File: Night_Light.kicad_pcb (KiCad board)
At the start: 2 copper layers, 27.9 x 27.9 mm, 10 parts, among them J1 3V0, Q1 2N3904

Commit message: Finished wiring the PCB
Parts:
- moved R3 0.25 mm to (128.8, 88.4)
- moved R2 0.22 mm to (145.9, 93.5)
- moved R1 0.14 mm to (128.8, 93.5)
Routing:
- net +3V0: track 0.00 -> 17.1 mm
- net /Base: track 0.00 -> 13.4 mm
- net /LED +: track 0.00 -> 5.40 mm
- net /Collecter: track 0.00 -> 4.98 mm
- added copper zone on B.Cu, net GND
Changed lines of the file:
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@@
   )
   (footprint "Resistor_THT:R_Axial_DIN0207_L6.3mm_D2.5mm_P10.16mm_Horizontal" (layer "F.Cu")
-    (at 128.524 88.392)
+    (at 128.778 88.392)
     (descr "Resistor, Axial_DIN0207 series, Axial, Horizontal, pin pitch=10.16mm, 0.25W = 1/4W, length*diameter=6.3*2.5mm^2, http://cdn-reichelt.de/documents/datenblatt/B400/1_4W%23YAG.pdf")
     (tags "Resistor Axial_DIN0207 series Axial Horizontal pin pitch 10.16mm 0.25W = 1/4W length 6.3mm diameter 2.5mm")
@@
   )
   (footprint "Resistor_THT:R_Axial_DIN0207_L6.3mm_D2.5mm_P10.16mm_Horizontal" (layer "F.Cu")
-    (at 128.92 93.5)
+    (at 128.778 93.472)
     (descr "Resistor, Axial_DIN0207 series, Axial, Horizontal, pin pitch=10.16mm, 0.25W = 1/4W, length*diameter=6.3*2.5mm^2, http://cdn-reichelt.de/documents/datenblatt/B400/1_4W%23YAG.pdf")
     (tags "Resistor Axial_DIN0207 series Axial Horizontal pin pitch 10.16mm 0.25W = 1/4W length 6.3mm diameter 2.5mm")
@@
   )
   (footprint "OptoDevice:R_LDR_4.9x4.2mm_P2.54mm_Vertical" (layer "F.Cu")
-    (at 145.94 93.25)
+    (at 145.94 93.472)
     (descr "Resistor, LDR 4.9x4.2mm")
     (tags "Resistor LDR4.9x4.2")
@@
   (gr_line (start 140.97 73.66) (end 140.97 106.68) (layer "Cmts.User") (width 0.15))
   (gr_rect (start 127 76.2) (end 154.94 104.14) (layer "Edge.Cuts") (width 0.1) (fill none))
+  (segment (start 145.96 86.348) (end 145.276 86.348) (width 0.5) (layer "F.Cu") (net 1))
+  (segment (start 145.276 86.348) (end 142.24 83.312) (width 0.5) (layer "F.Cu") (net 1))
+  (segment (start 139.7 83.312) (end 139.7 87.63) (width 0.5) (layer "F.Cu") (net 2))
+  (segment (start 139.7 87.63) (end 138.938 88.392) (width 0.5) (layer "F.Cu") (net 2))
+  (segment (start 137.97 100.584) (end 130.886 93.5) (width 0.5) (layer "F.Cu") (net 3))
+  (segment (start 128.778 93.472) (end 128.778 88.392) (width 0.5) (layer "F.Cu") (net 3))
+  (segment (start 130.886 93.5) (end 128.92 93.5) (width 0.5) (layer "F.Cu") (net 3))
+  (segment (start 145.94 88.908) (end 147.23 87.618) (width 0.5) (layer "F.Cu") (net 5))
+  (segment (start 145.94 93.472) (end 145.94 88.908) (width 0.5) (layer "F.Cu") (net 5))
+  (segment (start 138.938 93.472) (end 145.94 93.472) (width 0.5) (layer "F.Cu") (net 5))
+  (zone (net 4) (net_name "GND") (layer "B.Cu") (hatch edge 0.508)
+    (connect_pads (clearance 0.508))
+    (min_thickness 0.254) (filled_areas_thickness no)
+    (fill yes (thermal_gap 0.508) (thermal_bridge_width 0.508))
+    (polygon
+      (pts
+        (xy 157.48 106.68)
+        (xy 124.46 106.68)
+        (xy 124.46 73.66)
+        (xy 157.48 73.66)
+      )
+    )
+  )
 )

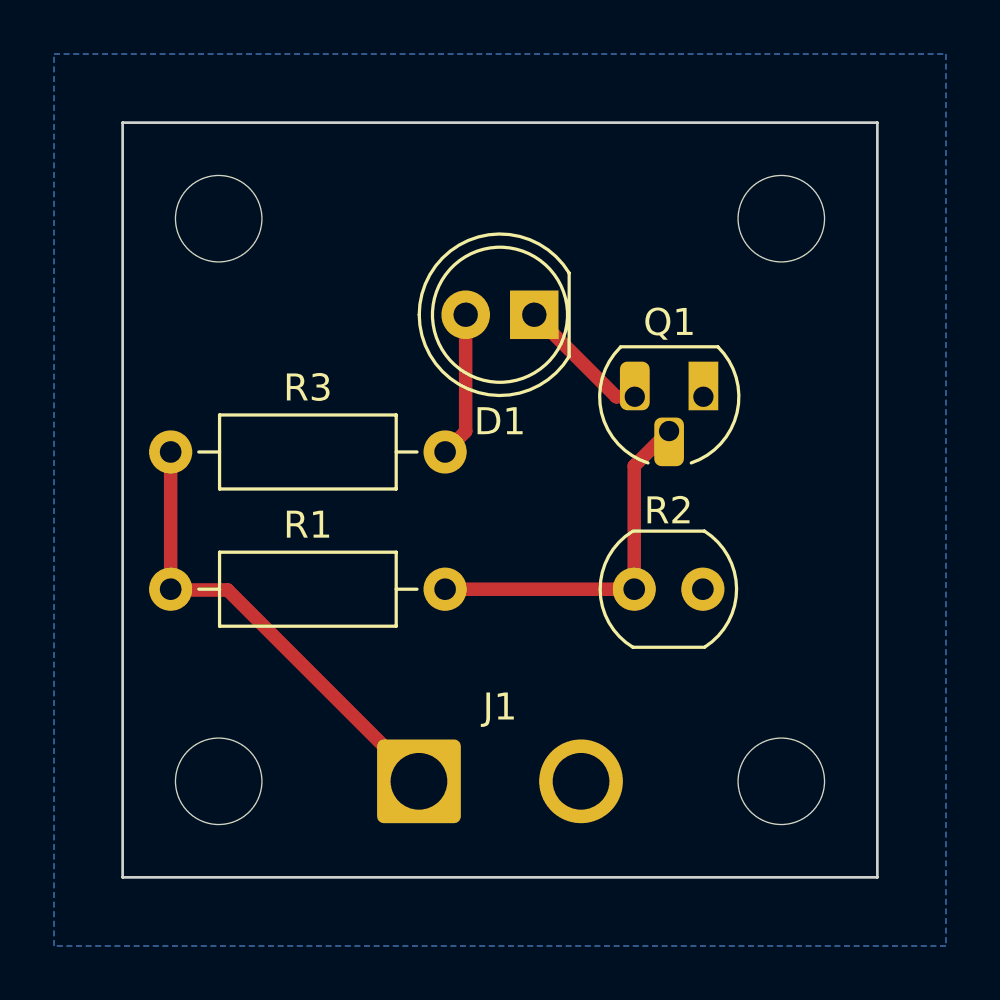
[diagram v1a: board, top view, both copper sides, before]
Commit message: Remove mounting holes. Reduce size to 1.0x1.0. Changed some footprints to match real board.
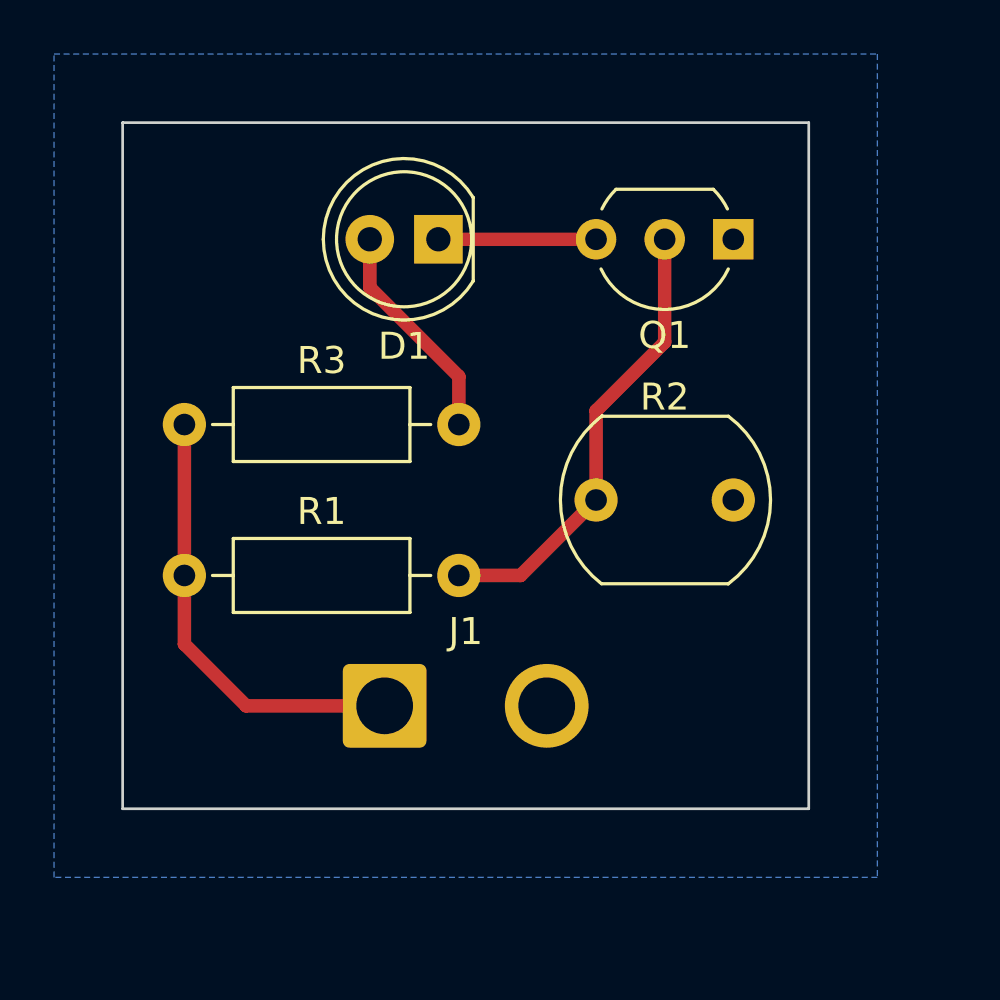
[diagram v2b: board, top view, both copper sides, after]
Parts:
- removed H1, H2, H3, H4: MountingHole, MountingHole:MountingHole_3.2mm_M3
- Q1: footprint Package_TO_SOT_THT:TO-92_HandSolder -> Package_TO_SOT_THT:TO-92_Inline_Wide
- R2: footprint OptoDevice:R_LDR_4.9x4.2mm_P2.54mm_Vertical -> OptoDevice:R_LDR_7x6mm_P5.1mm_Vertical
- moved Q1 5.93 mm to (149.6, 80.5)
- moved D1 4.52 mm to (138.7, 80.5)
- moved R2 3.59 mm to (144.5, 90.2)
- moved J1 3.07 mm to (136.7, 97.8)
- moved R3 1.14 mm to (129.3, 87.4)
- moved R1 0.72 mm to (129.3, 93.0)
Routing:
- net /Base: track 13.4 -> 16.9 mm
- net /LED +: track 5.40 -> 8.22 mm
- net /Collecter: track 4.98 -> 5.84 mm
- net +3V0: track 17.1 -> 16.5 mm
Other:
- board size 27.9 x 27.9 mm -> 25.4 x 25.4 mm

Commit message: Changed size of pads
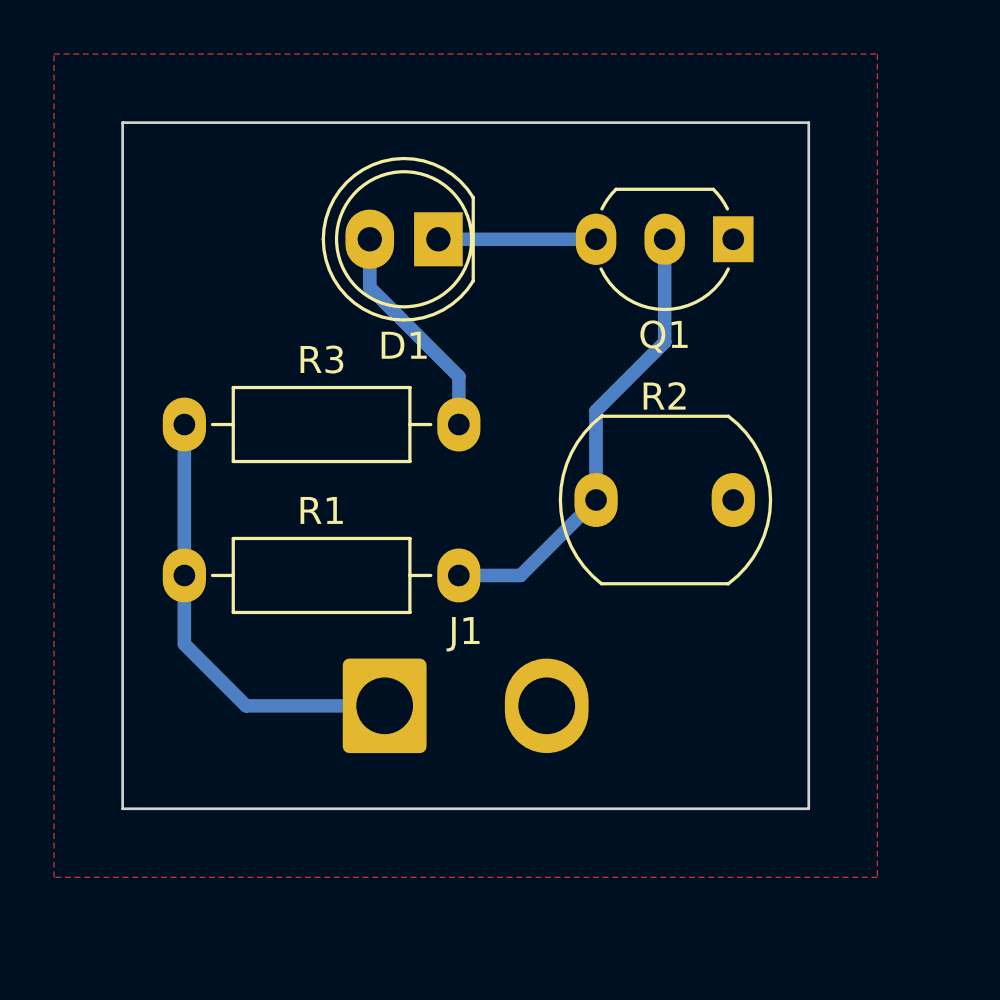
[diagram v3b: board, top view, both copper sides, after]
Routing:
- added copper zone on F.Cu, net GND
- removed copper zone on B.Cu, net GND
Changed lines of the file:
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@@
     (fp_arc (start -1.23 -1.469694) (mid 4.17 0.000016) (end -1.230016 1.469666) (layer "F.Fab") (width 0.1))
     (fp_circle (center 1.27 0) (end 3.77 0) (layer "F.Fab") (width 0.1) (fill none))
-    (pad "1" thru_hole rect (at 0 0 180) (size 1.8 1.8) (drill 0.9) (layers *.Cu *.Mask)
+    (pad "1" thru_hole rect (at 0 0 180) (size 1.8 2) (drill 0.9) (layers *.Cu *.Mask)
       (net 1 "/Collecter") (pinfunction "K") (pintype "passive"))
-    (pad "2" thru_hole circle (at 2.54 0 180) (size 1.8 1.8) (drill 0.9) (layers *.Cu *.Mask)
+    (pad "2" thru_hole oval (at 2.54 0 180) (size 1.8 2.2) (drill 0.9) (layers *.Cu *.Mask)
       (net 2 "/LED +") (pinfunction "A") (pintype "passive"))
     (model "${KICAD6_3DMODEL_DIR}/LED_THT.3dshapes/LED_D5.0mm_Clear.wrl"
@@
     (fp_line (start 10.16 0) (end 8.23 0) (layer "F.Fab") (width 0.1))
     (fp_line (start 1.93 1.25) (end 8.23 1.25) (layer "F.Fab") (width 0.1))
-    (pad "1" thru_hole circle (at 0 0) (size 1.6 1.6) (drill 0.8) (layers *.Cu *.Mask)
+    (pad "1" thru_hole oval (at 0 0) (size 1.6 2) (drill 0.8) (layers *.Cu *.Mask)
       (net 3 "+3V0") (pintype "passive"))
-    (pad "2" thru_hole oval (at 10.16 0) (size 1.6 1.6) (drill 0.8) (layers *.Cu *.Mask)
+    (pad "2" thru_hole oval (at 10.16 0) (size 1.6 2) (drill 0.8) (layers *.Cu *.Mask)
       (net 2 "/LED +") (pintype "passive"))
     (model "${KICAD6_3DMODEL_DIR}/Resistor_THT.3dshapes/R_Axial_DIN0207_L6.3mm_D2.5mm_P10.16mm_Horizontal.wrl"
@@
     (fp_arc (start 2.54 -2.48) (mid 4.831221 -0.949055) (end 4.293625 1.753625) (layer "F.Fab") (width 0.1))
     (fp_arc (start 0.786375 1.753625) (mid 0.248779 -0.949055) (end 2.54 -2.48) (layer "F.Fab") (width 0.1))
-    (pad "1" thru_hole rect (at 0 0 180) (size 1.5 1.5) (drill 0.8) (layers *.Cu *.Mask)
+    (pad "1" thru_hole rect (at 0 0 180) (size 1.5 1.7) (drill 0.8) (layers *.Cu *.Mask)
       (net 4 "GND") (pinfunction "E") (pintype "passive"))
-    (pad "2" thru_hole circle (at 2.54 0 180) (size 1.5 1.5) (drill 0.8) (layers *.Cu *.Mask)
+    (pad "2" thru_hole oval (at 2.54 0 180) (size 1.5 1.9) (drill 0.8) (layers *.Cu *.Mask)
       (net 5 "/Base") (pinfunction "B") (pintype "passive"))
-    (pad "3" thru_hole circle (at 5.08 0 180) (size 1.5 1.5) (drill 0.8) (layers *.Cu *.Mask)
+    (pad "3" thru_hole oval (at 5.08 0 180) (size 1.5 1.9) (drill 0.8) (layers *.Cu *.Mask)
       (net 1 "/Collecter") (pinfunction "C") (pintype "passive"))
     (model "${KICAD6_3DMODEL_DIR}/Package_TO_SOT_THT.3dshapes/TO-92_Inline_Wide.wrl"
@@
     (fp_circle (center 6 0) (end 7.5 0) (layer "F.Fab") (width 0.1) (fill none))
     (fp_circle (center 0 0) (end 1.5 0) (layer "F.Fab") (width 0.1) (fill none))
-    (pad "1" thru_hole roundrect (at 0 0) (size 3.1 3.1) (drill 2.1) (layers *.Cu *.Mask) (roundrect_rratio 0.080645)
+    (pad "1" thru_hole roundrect (at 0 0) (size 3.1 3.5) (drill 2.1) (layers *.Cu *.Mask) (roundrect_rratio 0.080645)
       (net 3 "+3V0") (pinfunction "Pin_1") (pintype "passive"))
-    (pad "2" thru_hole circle (at 6 0) (size 3.1 3.1) (drill 2.1) (layers *.Cu *.Mask)
+    (pad "2" thru_hole oval (at 6 0) (size 3.1 3.5) (drill 2.1) (layers *.Cu *.Mask)
       (net 4 "GND") (pinfunction "Pin_2") (pintype "passive"))
     (model "${KICAD6_3DMODEL_DIR}/Connector_Wire.3dshapes/SolderWire-1.5sqmm_1x02_P6mm_D1.7mm_OD3mm.wrl"
@@
     (fp_line (start 1.93 -1.25) (end 1.93 1.25) (layer "F.Fab") (width 0.1))
     (fp_line (start 8.23 -1.25) (end 1.93 -1.25) (layer "F.Fab") (width 0.1))
-    (pad "1" thru_hole circle (at 0 0) (size 1.6 1.6) (drill 0.8) (layers *.Cu *.Mask)
+    (pad "1" thru_hole oval (at 0 0) (size 1.6 2) (drill 0.8) (layers *.Cu *.Mask)
       (net 3 "+3V0") (pintype "passive"))
-    (pad "2" thru_hole oval (at 10.16 0) (size 1.6 1.6) (drill 0.8) (layers *.Cu *.Mask)
+    (pad "2" thru_hole oval (at 10.16 0) (size 1.6 2) (drill 0.8) (layers *.Cu *.Mask)
       (net 5 "/Base") (pintype "passive"))
     (model "${KICAD6_3DMODEL_DIR}/Resistor_THT.3dshapes/R_Axial_DIN0207_L6.3mm_D2.5mm_P10.16mm_Horizontal.wrl"
@@
     (fp_arc (start 4.84 -3) (mid 6.320211 -0.001572) (end 4.842494 2.998087) (layer "F.Fab") (width 0.1))
     (fp_arc (start 0.24 3) (mid -1.240211 0.001572) (end 0.237506 -2.998087) (layer "F.Fab") (width 0.1))
-    (pad "1" thru_hole circle (at 0 0) (size 1.6 1.6) (drill 0.8) (layers *.Cu *.Mask)
+    (pad "1" thru_hole oval (at 0 0) (size 1.6 2) (drill 0.8) (layers *.Cu *.Mask)
       (net 5 "/Base") (pintype "passive"))
-    (pad "2" thru_hole circle (at 5.08 0) (size 1.6 1.6) (drill 0.8) (layers *.Cu *.Mask)
+    (pad "2" thru_hole oval (at 5.08 0) (size 1.6 2) (drill 0.8) (layers *.Cu *.Mask)
       (net 4 "GND") (pintype "passive"))
     (model "${KICAD6_3DMODEL_DIR}/OptoDevice.3dshapes/R_LDR_7x6mm_P5.1mm_Vertical.wrl"
@@
   (gr_line (start 139.7 73.66) (end 139.7 106.68) (layer "Cmts.User") (width 0.15))
   (gr_rect (start 127 76.2) (end 152.4 101.6) (layer "Edge.Cuts") (width 0.1) (fill none))
-  (segment (start 138.689 80.518) (end 144.526 80.518) (width 0.5) (layer "F.Cu") (net 1))
-  (segment (start 136.149 82.301) (end 139.446 85.598) (width 0.5) (layer "F.Cu") (net 2))
-  (segment (start 139.446 85.598) (end 139.446 87.376) (width 0.5) (layer "F.Cu") (net 2))
-  (segment (start 136.149 80.518) (end 136.149 82.301) (width 0.5) (layer "F.Cu") (net 2))
-  (segment (start 129.286 92.964) (end 129.286 87.376) (width 0.5) (layer "F.Cu") (net 3))
-  (segment (start 129.286 95.504) (end 129.286 92.964) (width 0.5) (layer "F.Cu") (net 3))
-  (segment (start 136.7 97.79) (end 131.572 97.79) (width 0.5) (layer "F.Cu") (net 3))
-  (segment (start 131.572 97.79) (end 129.286 95.504) (width 0.5) (layer "F.Cu") (net 3))
-  (segment (start 139.446 92.964) (end 141.732 92.964) (width 0.5) (layer "F.Cu") (net 5))
-  (segment (start 147.066 80.518) (end 147.066 84.328) (width 0.5) (layer "F.Cu") (net 5))
-  (segment (start 141.732 92.964) (end 144.526 90.17) (width 0.5) (layer "F.Cu") (net 5))
-  (segment (start 147.066 84.328) (end 144.526 86.868) (width 0.5) (layer "F.Cu") (net 5))
-  (segment (start 144.526 86.868) (end 144.526 90.17) (width 0.5) (layer "F.Cu") (net 5))
-  (zone (net 4) (net_name "GND") (layer "B.Cu") (hatch edge 0.508)
+  (segment (start 138.689 80.518) (end 144.526 80.518) (width 0.5) (layer "B.Cu") (net 1))
+  (segment (start 136.149 82.301) (end 139.446 85.598) (width 0.5) (layer "B.Cu") (net 2))
+  (segment (start 139.446 85.598) (end 139.446 87.376) (width 0.5) (layer "B.Cu") (net 2))
+  (segment (start 136.149 80.518) (end 136.149 82.301) (width 0.5) (layer "B.Cu") (net 2))
+  (segment (start 129.286 92.964) (end 129.286 87.376) (width 0.5) (layer "B.Cu") (net 3))
+  (segment (start 129.286 95.504) (end 129.286 92.964) (width 0.5) (layer "B.Cu") (net 3))
+  (segment (start 136.7 97.79) (end 131.572 97.79) (width 0.5) (layer "B.Cu") (net 3))
+  (segment (start 131.572 97.79) (end 129.286 95.504) (width 0.5) (layer "B.Cu") (net 3))
+  (segment (start 139.446 92.964) (end 141.732 92.964) (width 0.5) (layer "B.Cu") (net 5))
+  (segment (start 147.066 80.518) (end 147.066 84.328) (width 0.5) (layer "B.Cu") (net 5))
+  (segment (start 141.732 92.964) (end 144.526 90.17) (width 0.5) (layer "B.Cu") (net 5))
+  (segment (start 147.066 84.328) (end 144.526 86.868) (width 0.5) (layer "B.Cu") (net 5))
+  (segment (start 144.526 86.868) (end 144.526 90.17) (width 0.5) (layer "B.Cu") (net 5))
+  (zone (net 4) (net_name "GND") (layer "F.Cu") (hatch edge 0.508)
     (connect_pads (clearance 0.508))
     (min_thickness 0.254) (filled_areas_thickness no)

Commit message: Updated silkscreen and version
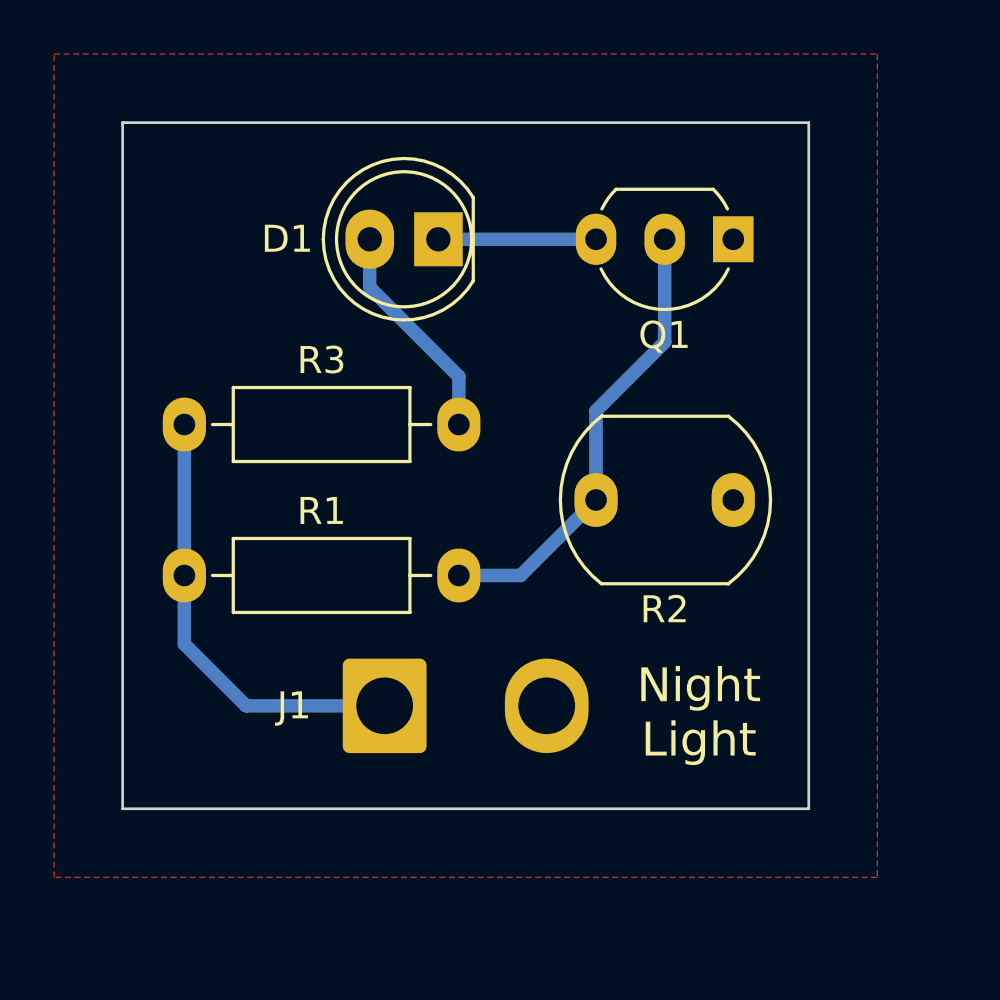
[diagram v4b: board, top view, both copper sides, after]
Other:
- board text added: "Designed by a Julian Jayhawk"
- board text added: "Night Light"
- board text added: "v1.0.0"
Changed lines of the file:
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@@
   )
   (paper "USLetter")
+  (title_block
+    (title "Night Light")
+    (date "2023-02-04")
+    (rev "1.0.0")
+    (company "Julian Jayhawks")
+    (comment 1 "Zach Dribin")
+  )
   (layers
     (0 "F.Cu" signal)
@@
     (property "Sheetname" "")
     (attr through_hole)
-    (fp_text reference "D1" (at 1.27 -3.96) (layer "F.SilkS")
+    (fp_text reference "D1" (at 5.593 0) (layer "F.SilkS")
       (effects (font (size 1 1) (thickness 0.15)))
     )
@@
     (property "Sheetname" "")
     (attr exclude_from_pos_files)
-    (fp_text reference "J1" (at 3 -2.75) (layer "F.SilkS")
+    (fp_text reference "J1" (at -3.35 0) (layer "F.SilkS")
       (effects (font (size 1 1) (thickness 0.15)))
     )
@@
     (property "Sheetname" "")
     (attr through_hole)
-    (fp_text reference "R2" (at 2.54 -3.81) (layer "F.SilkS")
+    (fp_text reference "R2" (at 2.54 4.064) (layer "F.SilkS")
       (effects (font (size 1 1) (thickness 0.15)))
     )
@@
   (gr_line (start 139.7 73.66) (end 139.7 106.68) (layer "Cmts.User") (width 0.15))
   (gr_rect (start 127 76.2) (end 152.4 101.6) (layer "Edge.Cuts") (width 0.1) (fill none))
+  (gr_text "v1.0.0" (at 148.336 98.044) (layer "B.SilkS")
+    (effects (font (size 1 1) (thickness 0.15)) (justify mirror))
+  )
+  (gr_text "Designed by a\nJulian Jayhawk" (at 139.7 84.074) (layer "B.SilkS")
+    (effects (font (size 1 1) (thickness 0.15)) (justify mirror))
+  )
+  (gr_text "Night\nLight" (at 148.336 98.044) (layer "F.SilkS")
+    (effects (font (size 1.25 1.25) (thickness 0.2)))
+  )
   (segment (start 138.689 80.518) (end 144.526 80.518) (width 0.5) (layer "B.Cu") (net 1))
   (segment (start 136.149 82.301) (end 139.446 85.598) (width 0.5) (layer "B.Cu") (net 2))
